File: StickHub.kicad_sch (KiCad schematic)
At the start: 94 parts, among them J1 HOST, J2 USB1, J3 USB2, J4 USB3, J5 USB4, J6 USB5, J7 USB6, J8 USB7, J9 EXTGND, U1 MaxLinear_XR22417-48, U2 Dialog_SLG5NT1487V, Y1 12MHz 50ppm 16-20pF

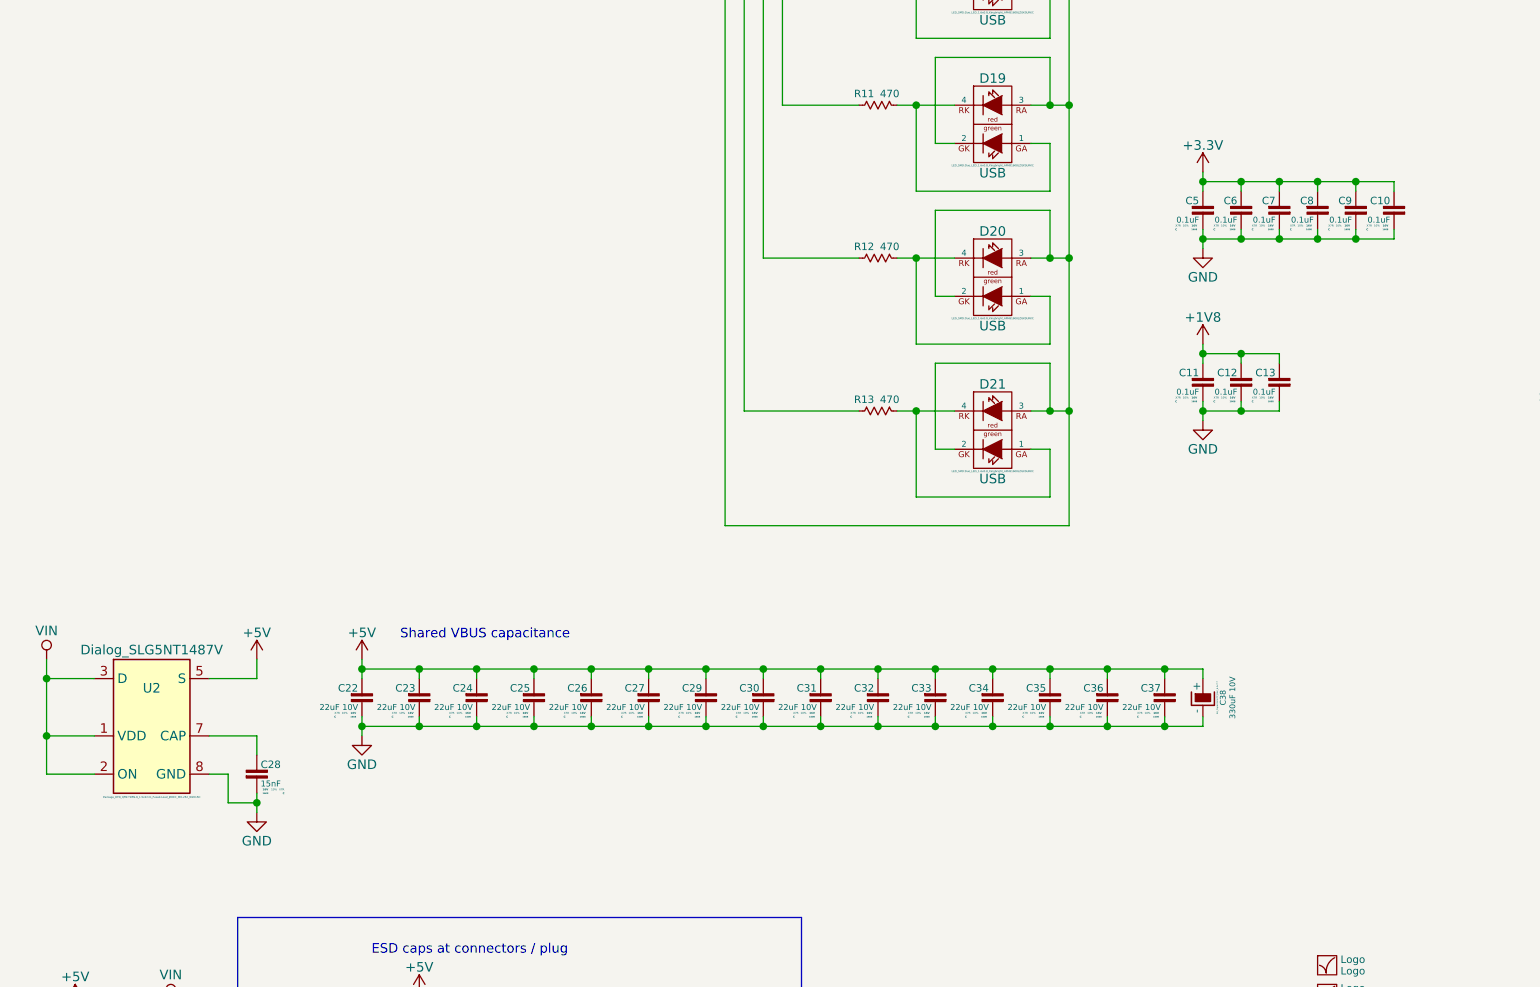
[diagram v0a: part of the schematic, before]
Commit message: Removing chunks of schematic and board.
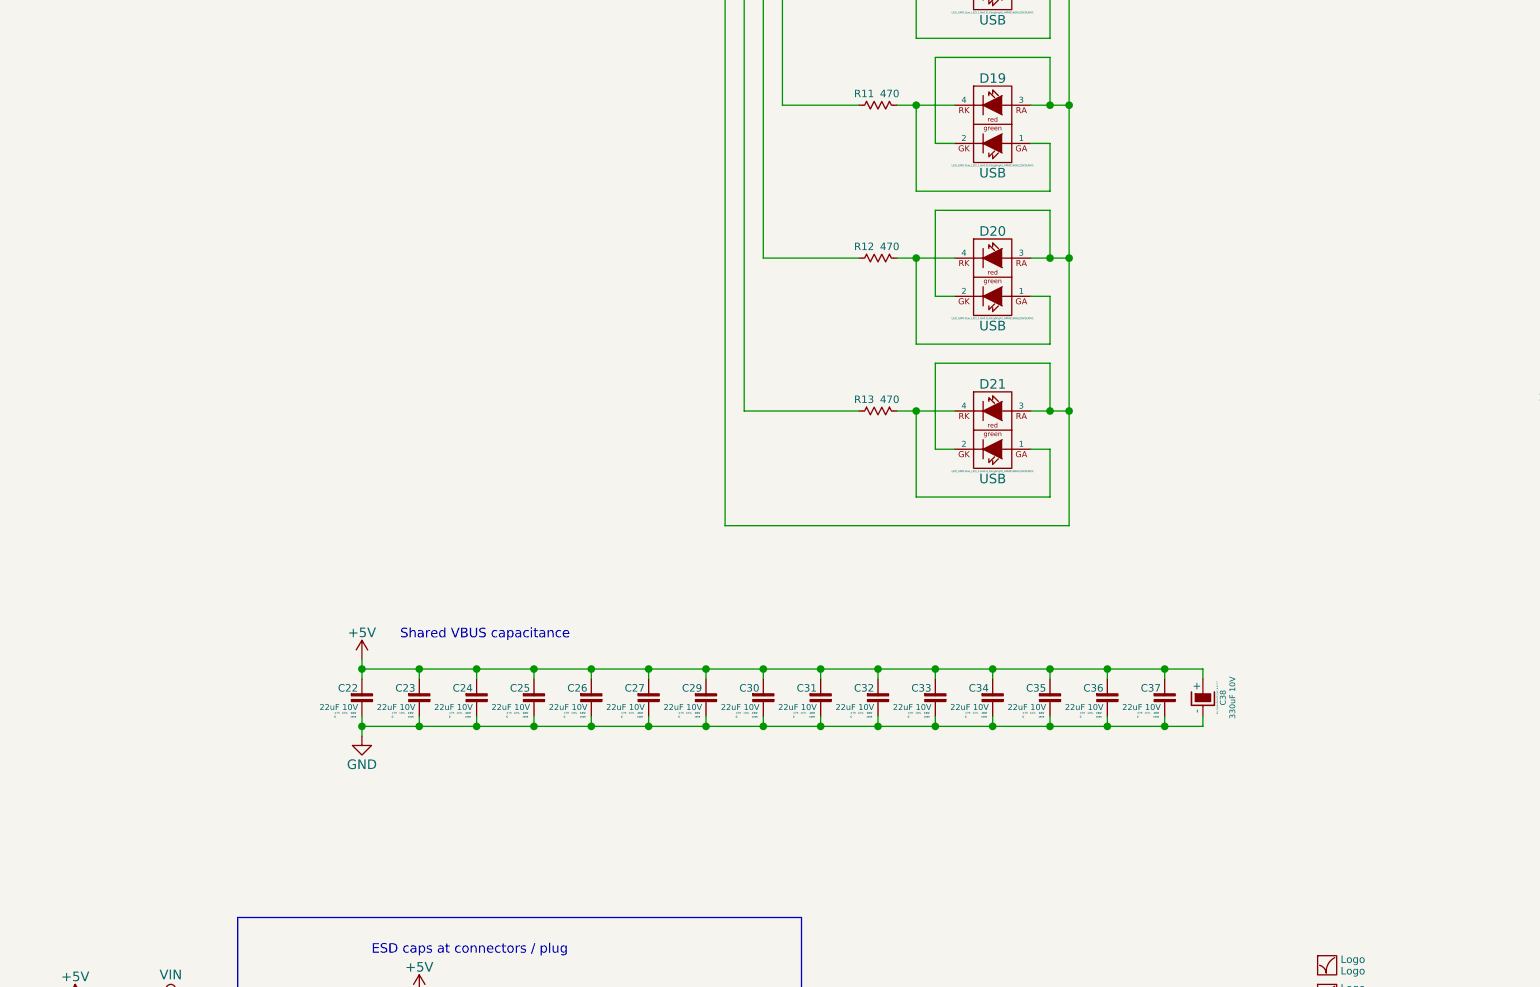
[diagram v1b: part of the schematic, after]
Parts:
- removed C10, C11, C12, C13, C5, C6, C7, C8, C9: 0.1uF, Capacitor_SMD:1608_C, symbol RobotProtos:Csmall
- removed C28: 15nF, Capacitor_SMD:1608_C, symbol RobotProtos:Csmall
- removed U2: Dialog_SLG5NT1487V, Package_DFN_QFN:TDFN-8_1.5x2mm_Fused-Lead_JEDEC_MO-252_W2015D, symbol RobotProtos:Dialog_SLG5NT1487V

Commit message: Revert "Removing chunks of schematic and board."
This reverts commit 6f6bff356a7eff26be86b812d608cab446a31a50.
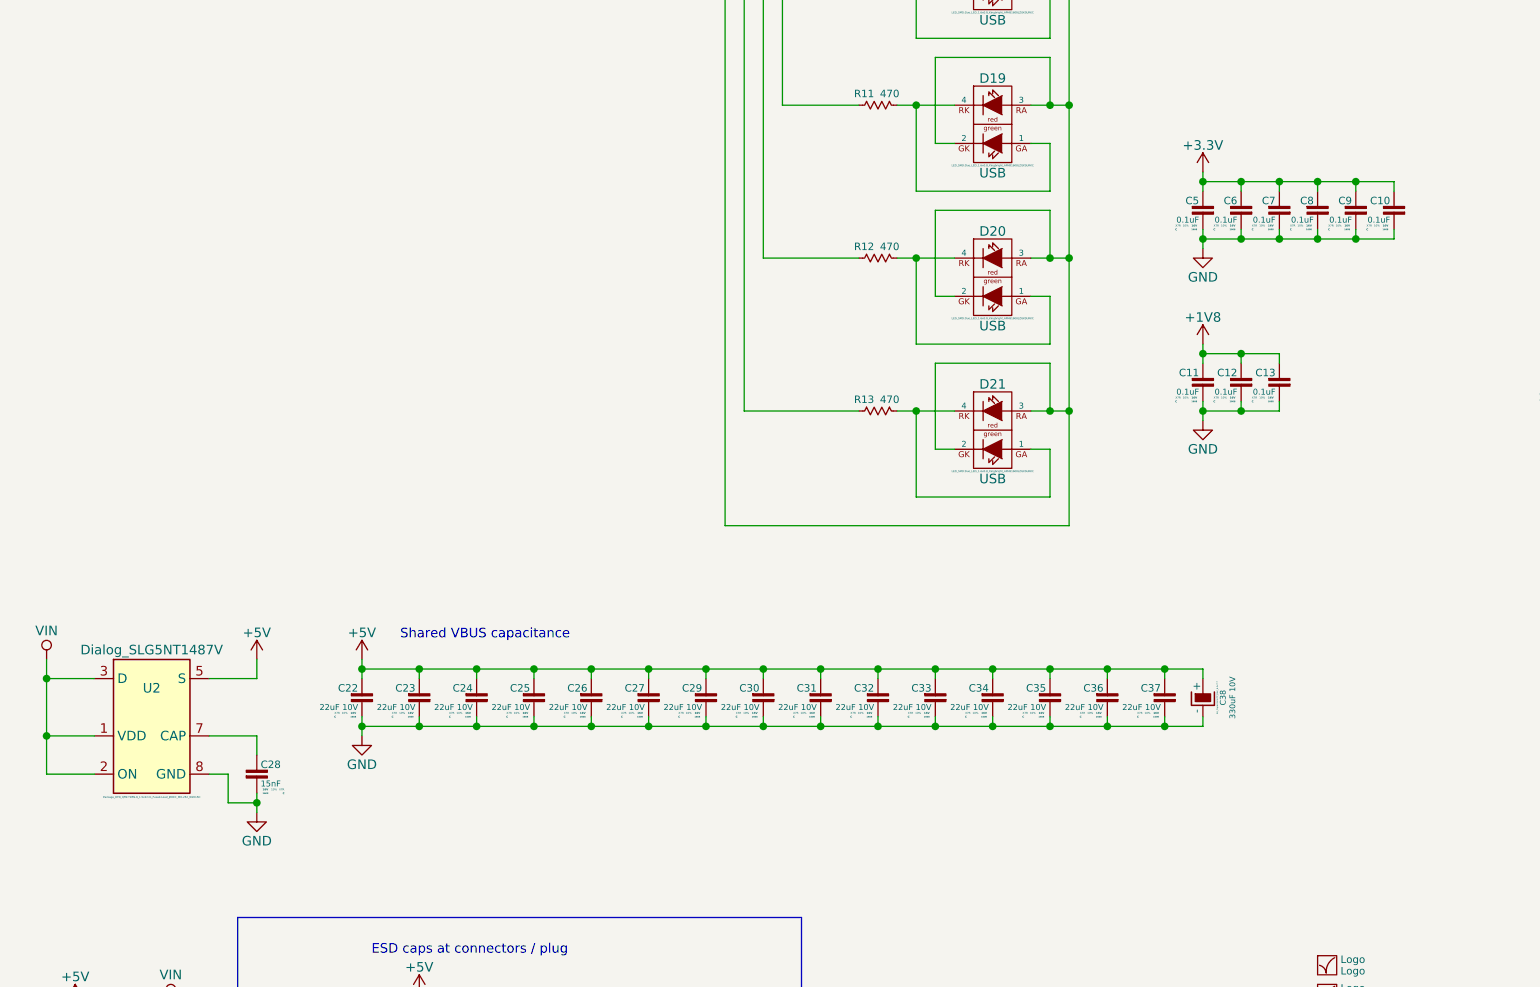
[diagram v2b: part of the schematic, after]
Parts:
- added C10, C11, C12, C13, C5, C6, C7, C8, C9: 0.1uF, Capacitor_SMD:1608_C, symbol RobotProtos:Csmall
- added C28: 15nF, Capacitor_SMD:1608_C, symbol RobotProtos:Csmall
- added U2: Dialog_SLG5NT1487V, Package_DFN_QFN:TDFN-8_1.5x2mm_Fused-Lead_JEDEC_MO-252_W2015D, symbol RobotProtos:Dialog_SLG5NT1487V
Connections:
- net +1V8: now also C11.1, C12.1, C13.1
- net +3.3V: now also C10.1, C5.1, C6.1, C7.1, C8.1, C9.1
- net +5V: now also U2.5 (S)
- net GND: now also C10.2, C11.2, C12.2, C13.2, C28.2, C5.2, C6.2, C7.2, C8.2, C9.2, U2.8 (GND)
- net VIN: now also U2.1 (VDD), U2.2 (ON), U2.3 (D)
- new net: C28.1, U2.7 (CAP)
